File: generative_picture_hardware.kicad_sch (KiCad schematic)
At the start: 40 parts

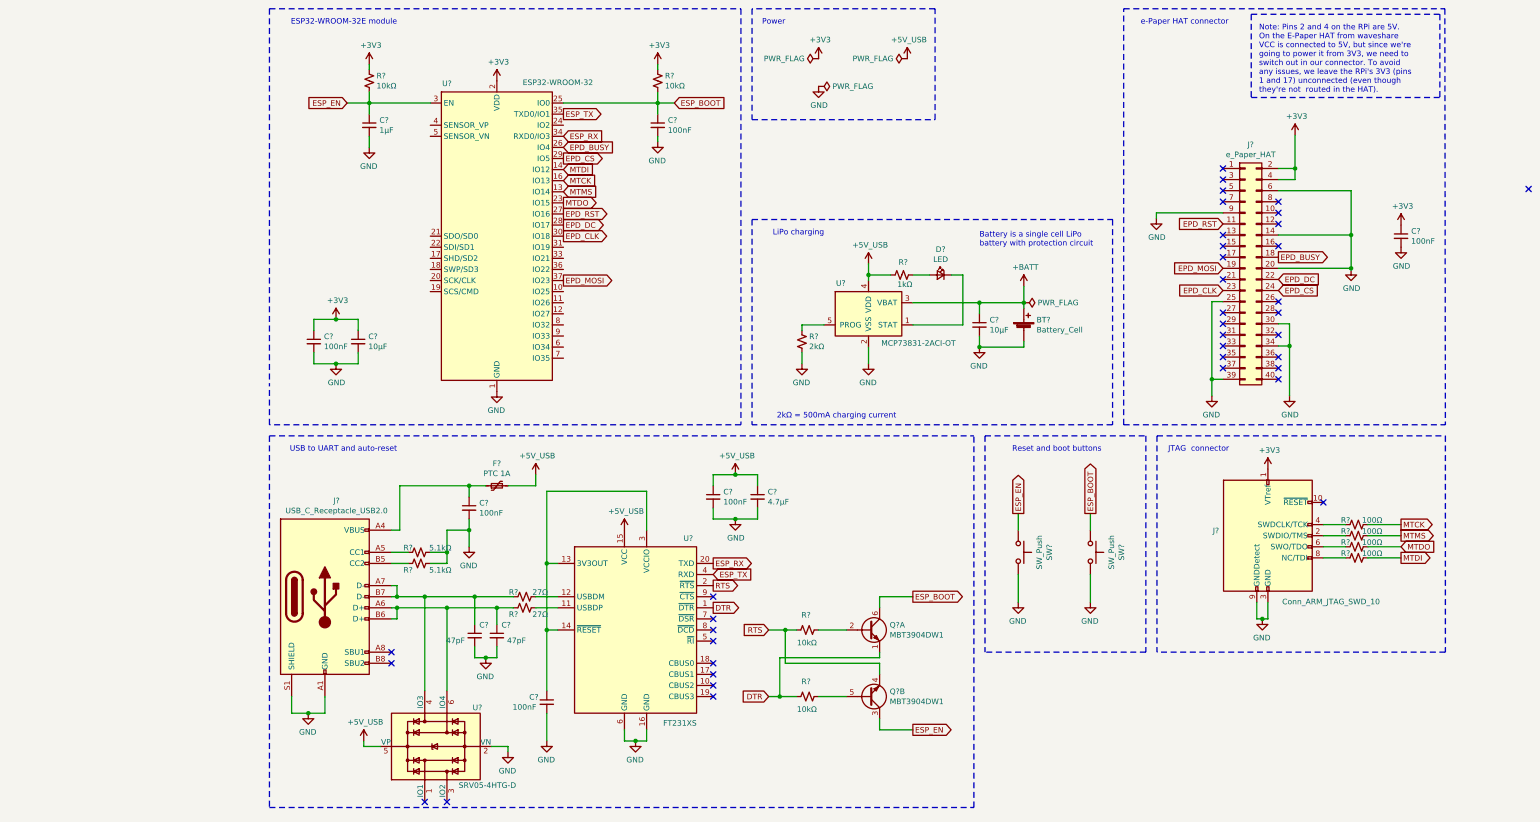
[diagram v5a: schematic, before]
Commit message: Adds LDO regulator circuit
This circuit uses a p-channel MOSFET to switch the power supply to the
regulator from battery to USB when the cable is plugged in[1].

[1]: https://www.youtube.com/watch?v=GRd9uTwg7r4
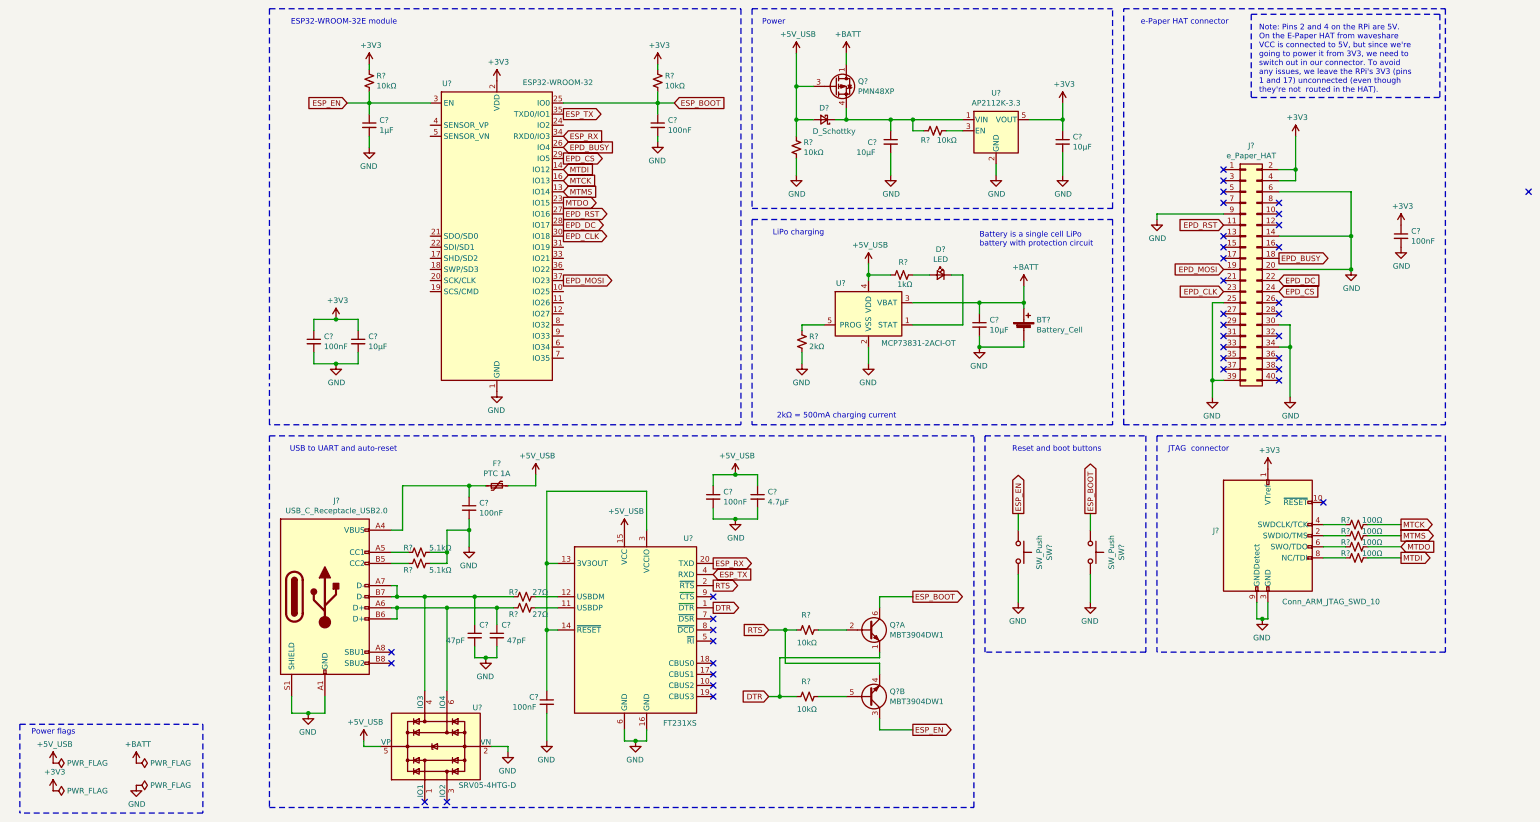
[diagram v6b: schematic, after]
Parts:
- added C? (x2): 10µF, symbol Device:C_Small
- added D?: D_Schottky, symbol Device:D_Schottky_Small
- added Q?: PMN48XP, Package_SO:TSOP-6_1.65x3.05mm_P0.95mm, symbol Transistor_FET:PMN48XP
- added R? (x2): 10kΩ, symbol Device:R_Small_US
- added U?: AP2112K-3.3, Package_TO_SOT_SMD:SOT-23-5, symbol Regulator_Linear:AP2112K-3.3
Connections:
- net +3V3: now also C?.1, U?.5 (VOUT)
- net +5V: now also D?.2 (A), Q?.3 (G), R?.1
- net +BATT: now also Q?.1 (D), Q?.2 (D), Q?.5 (D), Q?.6 (D)
- net GND: now also C?.2, C?.2, R?.2, U?.2 (GND)
- new net: C?.1, D?.1 (K), Q?.4 (S), R?.1, U?.1 (VIN)
- new net: R?.2, U?.3 (EN)
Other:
- note added: "Power flags"

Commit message: Adds annotations and fixes small issues after ERC
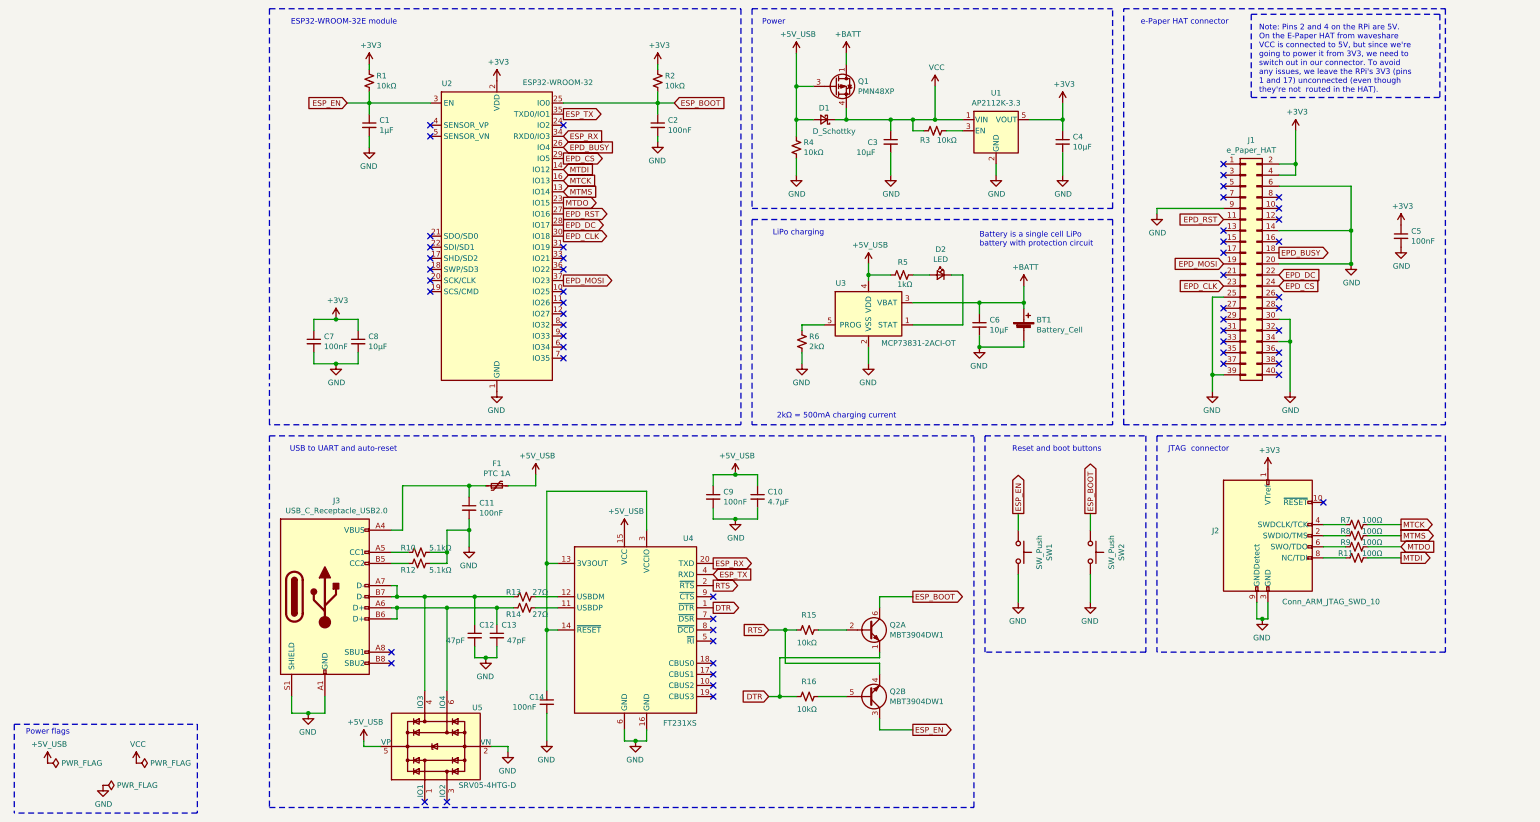
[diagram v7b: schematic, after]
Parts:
- gave numbers to parts that had none: 46
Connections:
- net VCC: now reaches C3.1, D1.1 (K), Q1.4 (S), R3.1, U1.1 (VIN)
- no-connect marks 38 -> 56
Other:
- moved on the sheet: J1
